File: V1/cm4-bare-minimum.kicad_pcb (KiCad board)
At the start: 2 copper layers, 120 x 40 mm, 38 parts, among them J1 Molex 470531000, J2 USB_OTG, J3 Micro_SD_Card_Det, J4 USB4105-GF-A, J5 Conn_01x03, J6 Conn_01x03, J7 THD-02-R, U1 TPD2EUSB30, U2 EMC2301-1-ACZL-TR, U3 RT9742GGJ5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

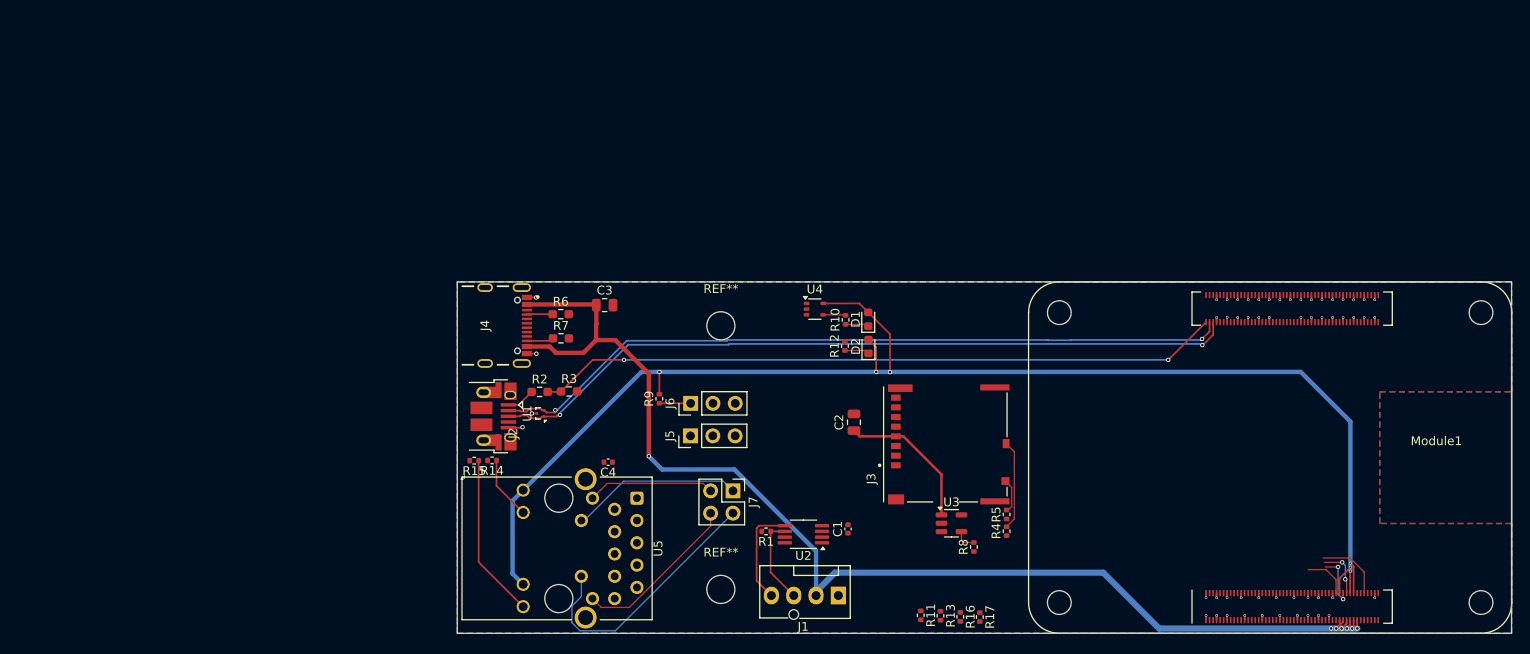
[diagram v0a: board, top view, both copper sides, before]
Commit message: Completed V1, Generated Output Files
Finished PCB layout, fixed all design rule violations and completed the design. Gerber files, Drill files, Bill of Materials, generated.
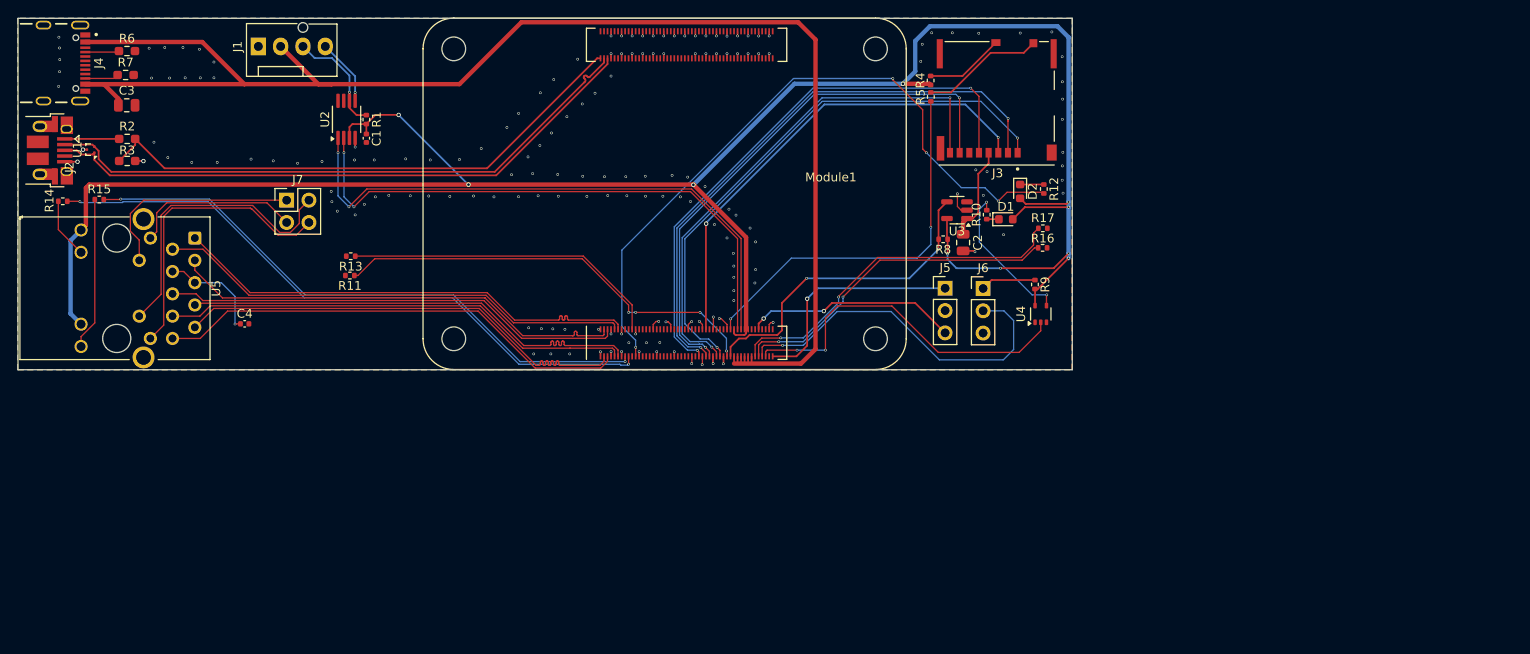
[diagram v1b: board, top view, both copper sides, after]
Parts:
- removed REF** (x2): MountingHole_3.2mm_M3, MountingHole:MountingHole_3.2mm_M3
- moved J1 90.9 mm to (67.4, 53.2), turned to 0 degrees
- moved R13 78.6 mm to (77.9, 77.1), turned to 180 degrees
- moved R11 75.6 mm to (77.8, 79.3), turned to 180 degrees
- moved Module1 75.2 mm to (141.1, 90.0)
- moved C1 70.6 mm to (79.7, 63.6), turned to -90 degrees
- moved U2 70.2 mm to (77.4, 61.5), turned to 90 degrees
- moved R1 65.3 mm to (79.7, 61.5), turned to -90 degrees
- moved J7 60.6 mm to (70.6, 70.7), turned to 0 degrees
- moved U1 59.4 mm to (48.3, 64.9)
- moved C3 59.0 mm to (52.4, 59.9)
- moved J2 58.9 mm to (42.5, 65.0)
- moved J4 58.5 mm to (42.9, 55.1)
- moved U5 58.4 mm to (51.2, 80.7)
- moved R7 57.9 mm to (52.2, 56.5)
- moved R6 57.7 mm to (52.4, 53.7)
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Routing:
- net /CM4_3V3: track 160.3 -> 247.9 mm, vias 6 -> 10
- net /PI_nLED_Activity: track 0.00 -> 77.8 mm, vias 0 -> 4
- net /ETH_LEDG: track 0.00 -> 72.6 mm, vias 0 -> 2
- net /ETH_LEDY: track 0.00 -> 67.6 mm, vias 0 -> 2
- net /SD_DAT3: track 0.00 -> 66.1 mm, vias 0 -> 2
- net /SD_CLK: track 0.00 -> 64.6 mm, vias 0 -> 2
- net /SD_DAT2: track 0.00 -> 63.4 mm, vias 0 -> 2
- net /SD_DAT0: track 0.00 -> 61.4 mm, vias 0 -> 2
- net /SDA0: track 5.75 -> 66.5 mm
- net /SD_DAT1: track 0.00 -> 59.5 mm, vias 0 -> 2
- net /SCL0: track 6.03 -> 65.2 mm
- net /TRD0_N: track 0.00 -> 54.4 mm
- net /TRD3_N: track 0.00 -> 54.4 mm
- net /TRD0_P: track 0.00 -> 54.4 mm
- net /SD_CMD: track 0.00 -> 54.3 mm, vias 0 -> 2
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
